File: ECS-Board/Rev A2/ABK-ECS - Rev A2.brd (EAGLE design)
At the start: 100 x 80 mm, 242 parts, among them J1 22-27-2061-06, J10 22-05-7068-06, J2 USB-B-S-RA, J3 1241050-5, J4 MSTBA2, J5 22-05-7068-06, J6 22-05-7028-02, J7 22-05-7058-05, J8 22-05-7068-06, J9 22-05-7028-02, K1 G6K-2G-Y, SW1 B3FS-1015, SW2 B3FS-1015, T1 EXMACHINA-LOGO-NAME, T10 MMBT2222AL, T11 MMBT2222AL, T12 IRLML5103TRPBF, T13 IRLML5103TRPBF, T14 IRLML5103TRPBF, T15 IRLML5103TRPBF, T16 MMBT2222AL, T17 MMBT2222AL, T18 MMBT2222AL, T19 MMBT2222AL, T2 IRLML5103TRPBF, T3 MMBT2222AL, T4 IRLML5103TRPBF, T5 IRLML5103TRPBF, T6 IRLML5103TRPBF, T7 IRLML5103TRPBF, T8 MMBT2222AL, T9 MMBT2222AL, U1 AT24C512C-SSHM-B, U2 LPC1768FBD100, U3 LT3686HDDPBF, U4 LT3686HDDPBF, U5 SN74LVC2G17DBVR, U6 SN74LVC2G17DBVR, U7 SN74LVC2G17DBVR, U8 SN74LVC2G17DBVR, U9 TC1264-3.3, X1 FC-135, X2 ASE-12, X3 3000

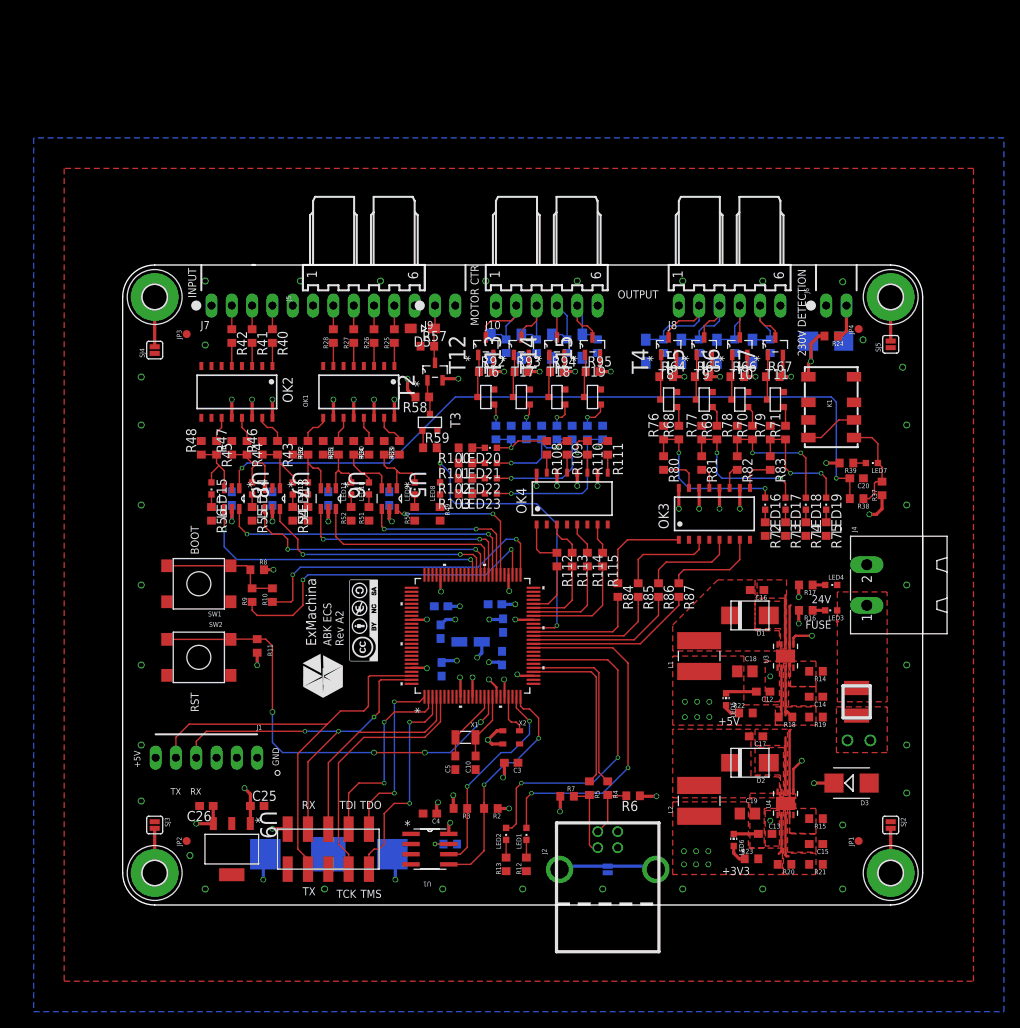
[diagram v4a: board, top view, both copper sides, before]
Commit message: Add pullup resistor on AT24C WP Separate +5V from ISP connector and the +5V general and add a diode Change +5V--->+3V3 conversion methode on input Wired OK2D
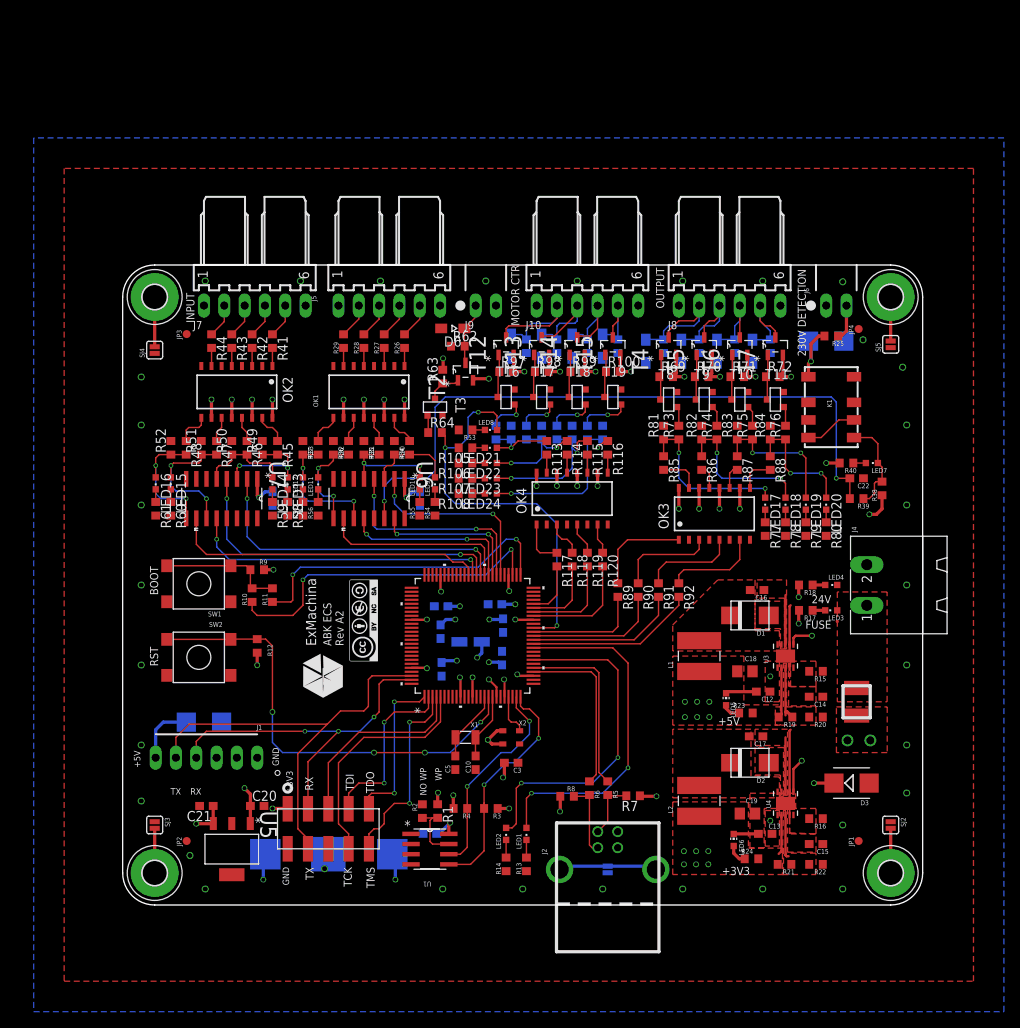
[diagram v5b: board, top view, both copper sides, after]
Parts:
- removed C25, C26: 1u, rcl:C0603
- removed U8: SN74LVC2G17DBVR, ti:SOT95P280X145-6N
- removed U9: TC1264-3.3, microchip-6:SOT230P700X180-4N
- added D14: 1N4148WS, diode:SOD323-W
- added LED24: Blue, led:CHIPLED_0603
- added R116: 1K, rcl:R0603
- added R117, R118, R119, R120: 330, rcl:R0603
- C20, C21: value 0.1uF -> 1u
- D5: value 1N4148WS -> STPS3L40UF; device diode:SOD323-W -> diode:SMB
- J7: value 22-05-7058-05 -> 22-05-7068-06; device con-molex:7395-05 -> con-molex:7395-06
- R100, R72: value 1K5 -> 330
- R101, R102, R103, R39, R73, R74, R75: value 1K5 -> 100
- R104, R76: value 4K7 -> 100
- R105, R106, R107, R77, R78, R79: value 4K7 -> 1K5
- R108, R40, R80: value 1K -> 1K5
- R109, R110, R111, R81, R82, R83: value 1K -> 4K7
- R11: value 10K -> 0R
- R112, R84: value 330 -> 4K7
- R113, R114, R115, R85, R86, R87: value 330 -> 1K
- R12, R22: value 1K5 -> 10K
- R14: value 31K6 -> 1K5
- R16: value 4K7 -> 31K6
- R18: value 52K3 -> 4K7
- R19: value 10K -> 52K3
- R20: value 31K6 -> 10K
- R21: value 10K -> 31K6
- R24, R59: value 100 -> 1K5
- R25: value 1K -> 100
- R33, R46, R47, R48: value 4K7 -> 1K
- R38: value 100 -> 4K7
- R4: value 33 -> 4K7
- R49, R50, R51, R52: value 1K5 -> 4K7
- R57, R60, R61, R8: value 10K -> 1K5
- R58: value 330 -> 1K5
- R6: value 1K5 -> 33
- R63, R89, R90, R91: value 10K -> 330
- R64: value 330 -> 100
- R65, R66, R67, R93, R94, R95: value 330 -> 10K
- R68, R96: value 100 -> 10K
- R69, R70, R71, R97, R98, R99: value 100 -> 330
- R88: value 10K -> 1K
- R9: value 0R -> 10K
- U5: value SN74LVC2G17DBVR -> TC1264-3.3; device ti:SOT95P280X145-6N -> microchip-6:SOT230P700X180-4N
- U6, U7: value SN74LVC2G17DBVR -> CD4050BD; device ti:SOT95P280X145-6N -> ti:SOIC127P600X175-16N
- moved D4 91.2 mm to (10.2, 22.9)
- moved C20 85.4 mm to (16.8, 12.4)
- moved C22 78.1 mm to (91.7, 53.3), flipped to the top, turned to 0 degrees
- moved LED16 76.2 mm to (4.13, 52.7)
- moved R40 73.5 mm to (90.5, 55.2), turned to 180 degrees
- moved R37 72.6 mm to (22.5, 57.1)
- moved R61 70.9 mm to (4.13, 49.5), flipped to the top, turned to 270 degrees
- moved R24 66.1 mm to (78.6, 5.78), turned to 0 degrees
- moved R60 64.9 mm to (6.02, 49.5), flipped to the top, turned to 270 degrees
- moved R25 54.6 mm to (88.6, 71.1), turned to 180 degrees
- moved D5 50.5 mm to (87.9, 70.5), flipped to the bottom
- moved U5 48.0 mm to (13.6, 6.99)
- moved R8 48.0 mm to (55.5, 13.6)
- moved R14 45.6 mm to (47.9, 5.08), turned to 270 degrees
- moved C21 44.7 mm to (10.5, 12.4), flipped to the top, turned to 180 degrees
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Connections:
- removed net INPUT: LED15.A, R45.2, R48.1, U8.3
- removed net INPUT_MCU: U2.63, U8.4
- new net +5V/1: C20.1, D4.C, J1.6, U5.1
- new net INPUT1: LED15.A, R47.2, R51.1, U7.11
- new net INPUT1_MCU: U2.63, U7.12
- new net INPUT2: LED16.A, R48.2, R52.1, U7.9
- new net INPUT2_MCU: U2.64, U7.10
- new net N$110: OK2.9, R48.1
- new net N$111: OK2.7, R44.2
- new net N$112: J7.2, R44.1
- new net N$90: LED16.C, R61.1
- net !RESET: now also R12.1; no longer R11.1
- net +24V: now also R100.2, R18.2, R63.2, R69.2, R70.2, R71.2, R72.2, R97.2, R98.2, R99.2; no longer R16.2, R58.2, R64.2, R65.2, R66.2, R67.2, R92.2, R93.2, R94.2, R95.2
- net +3V3: now also R1.1, R12.2, R21.2, R24.2, R4.2, R8.1, R9.2, U5.3, U6.1, U7.1; no longer C22.1, C26.1, R11.2, R2.2, R20.2, R23.2, R6.1, R8.2, U5.5, U6.5, U7.5, U8.5, U9.3
- net +5V: now also OK2.10, R19.2, R23.2, R38.1, R40.2; no longer C25.1, J1.6, R18.2, R22.2, R37.1, R39.2, U9.1
- net 230V_DETECTION: now also C22.1, R39.2, U6.14; no longer C20.1, R38.2, U8.1
- net 230V_DETECTION_MCU: now also U6.15; no longer U8.6
- net BOOT_SELECT_P2_10: now also R10.1; no longer R9.1
- net BOOT_SELECT_P2_12: now also R11.1; no longer R10.1
- net BRAKE_CONTROL: now also D10.C, R68.2; no longer D9.C, R63.2
- net BRAKE_CONTROL_MCU: now also R92.2; no longer R87.2
- net CLUTCH_CONTROL: now also D9.C, R67.2; no longer D8.C, R62.2
- net CLUTCH_CONTROL_MCU: now also R91.2; no longer R86.2
- net DRIVE_STATUS_1: now also R32.2, R36.1, U6.9; no longer R31.2, R35.1, U6.1
- net DRIVE_STATUS_1_MCU: now also U6.10; no longer U6.6
- net DRIVE_STATUS_2: now also R33.2, R37.1, U6.11; no longer R32.2, R36.1, U6.3
- net DRIVE_STATUS_2_MCU: now also U6.12; no longer U6.4
- net EEPROM_SCL: now also R4.1; no longer R3.1
- net EEPROM_SDA: now also R3.1; no longer R2.1
- net EMERGENCY_STOP: now also R30.2, R34.1, U6.3; no longer R29.2, R33.1, U5.1
- net EMERGENCY_STOP_MCU: now also U6.2; no longer U5.6
- net GND: now also D14.A, J7.6, OK2.8, R108.2, R109.2, R110.2, R111.2, R112.2, R14.2, R16.1, R2.2, R20.1, R22.1, R37.2, R57.2, R58.2, R59.2, R60.2, R61.2, R65.1, R66.1, R67.1, R68.1, R80.2, R81.2, R82.2, R83.2, R84.2, R93.1, R94.1, R95.1, R96.1, U5.4, U6.8, U7.8; no longer C25.2, C26.2, J7.5, R1.2, R100.2, R101.2, R102.2, R103.2, R104.2, R12.2, R14.1, R19.1, R21.1, R33.2, R46.2, R47.2, R48.2, R57.1, R60.1, R61.1, R63.1, R72.2, R73.2, R74.2, R75.2, R76.2, R88.1, R89.1, R90.1, R91.1, U6.2, U7.2, U8.2, U9.2, U9.4
- net LED1: now also D11.C, R93.2; no longer D10.C, R88.2
- net LED1_MCU: now also R117.2; no longer R112.2
- net LED2: now also D12.C, R94.2; no longer D11.C, R89.2
- net LED2_MCU: now also R118.2; no longer R113.2
- net LED3: now also D13.C, R95.2; no longer D12.C, R90.2
- net LED3_MCU: now also R119.2; no longer R114.2
- net LED4: now also D14.C, R96.2; no longer D13.C, R91.2
- net LED4_MCU: now also R120.2; no longer R115.2
- net LIMIT_SWITCH: now also R31.2, R35.1, U6.5; no longer R30.2, R34.1, U5.3
- net LIMIT_SWITCH_MCU: now also U6.4; no longer U5.4
- net L_VALIDATION: now also D8.C, R66.2; no longer D7.C, R61.2
- net L_VALIDATION_MCU: now also R90.2; no longer R85.2
- net MOTOR_CONTROL_MCU: now also R64.2; no longer R59.2
- net N$1: now also R6.1, R8.2; no longer R5.1, R7.2
- net N$100: now also R45.1; no longer R43.1
- net N$101: now also R42.2; no longer R41.2
- net N$102: now also J7.4, R42.1; no longer J7.3, R41.1
- net N$103: now also R46.1; no longer R44.1
- net N$104: now also R43.2; no longer R42.2
- net N$105: now also J7.3, R43.1; no longer J7.2, R42.1
- net N$106: now also R47.1; no longer R45.1
- net N$107: now also R58.1; no longer R54.1
- net N$108: now also R59.1; no longer R55.1
- net N$109: now also R60.1; no longer R56.1
- net N$13: now also R21.1, R22.2; no longer R20.1, R21.2
- net N$17: now also R73.2; no longer R68.2
- net N$18: now also R69.1; no longer R64.1
- net N$19: now also R74.2; no longer R69.2
- net N$2: now also R5.1, R7.2; no longer R4.1, R6.2
- net N$20: now also R70.1; no longer R65.1
- net N$21: now also R75.2; no longer R70.2
- net N$22: now also R71.1; no longer R66.1
- net N$23: now also R76.2; no longer R71.2
- net N$24: now also R72.1; no longer R67.1
- net N$25: now also R64.1; no longer R59.1
- net N$26: now also R63.1; no longer R58.1
- net N$27: now also R1.2, R2.1; no longer R1.1
- net N$28: now also D5.C, R25.2; no longer D4.C, R24.2
- net N$29: now also R13.1; no longer R12.1
- net N$3: now also R14.1; no longer R13.1
- net N$30: now also D6.C, R62.2; no longer D5.C, R57.2
- net N$31: now also LED21.A, R101.1, R109.1, R113.1; no longer LED20.A, R104.1, R108.1, R96.1
- net N$32: now also R25.1; no longer R24.1
- net N$33: now also R113.2; no longer R108.2
- net N$34: now also LED22.A, R102.1, R110.1, R114.1; no longer LED21.A, R105.1, R109.1, R97.1
- net N$35: now also R114.2; no longer R109.2
- net N$36: now also LED23.A, R103.1, R111.1, R115.1; no longer LED22.A, R106.1, R110.1, R98.1
- net N$37: now also LED24.A, R104.1, R112.1, R116.1; no longer LED23.A, R107.1, R111.1, R99.1
- net N$38: now also R115.2; no longer R110.2
- net N$39: now also R116.2; no longer R111.2
- net N$4: now also R15.2; no longer R14.2
- net N$40: now also R117.1; no longer R112.1
- net N$41: now also R26.2; no longer R25.2
- net N$42: now also R118.1; no longer R113.1
- net N$43: now also R120.1; no longer R115.1
- net N$44: now also R18.1; no longer R17.1
- net N$45: now also R17.1; no longer R16.1
- net N$46: now also R119.1; no longer R114.1
- net N$47: now also R27.2; no longer R26.2
- net N$48: now also R28.2; no longer R27.2
- net N$49: now also R29.2; no longer R28.2
- net N$5: now also R11.2, R9.1; no longer R8.1, R9.2
- net N$50: now also R24.1; no longer R23.1
- net N$51: now also R23.1; no longer R22.1
- net N$52: now also R29.1; no longer R28.1
- net N$53: now also R28.1; no longer R27.1
- net N$54: now also R27.1; no longer R26.1
- net N$55: now also R26.1; no longer R25.1
- net N$56: now also R53.1; no longer R49.1
- net N$57: now also R54.1; no longer R50.1
- net N$58: now also R55.1; no longer R51.1
- net N$59: now also R56.1; no longer R52.1
- net N$61: now also R33.1; no longer R32.1
- net N$62: now also R32.1; no longer R31.1
- net N$63: now also R31.1; no longer R30.1
- net N$64: now also R30.1; no longer R29.1
- net N$65: now also R57.1; no longer R53.1
- net N$66: now also LED21.C, R105.1; no longer LED20.C, R100.1
- net N$67: now also LED22.C, R106.1; no longer LED21.C, R101.1
- net N$68: now also LED23.C, R107.1; no longer LED22.C, R102.1
- net N$69: now also LED24.C, R108.1; no longer LED23.C, R103.1
- net N$7: now also R16.2; no longer R15.2
- net N$71: now also R97.1; no longer R92.1
- net N$72: now also R98.1; no longer R93.1
- net N$73: now also R38.2, R39.1; no longer R37.2, R38.1
- net N$74: now also R40.1; no longer R39.1
- net N$75: now also LED17.A, R73.1, R81.1, R85.1; no longer LED16.A, R68.1, R76.1, R80.1
- net N$76: now also R85.2; no longer R80.2
- net N$77: now also R99.1; no longer R94.1
- net N$78: now also R100.1; no longer R95.1
- net N$79: now also LED18.A, R74.1, R82.1, R86.1; no longer LED17.A, R69.1, R77.1, R81.1
- net N$80: now also R86.2; no longer R81.2
- net N$81: now also R41.2; no longer R40.2
- net N$82: now also J7.5, R41.1; no longer J7.4, R40.1
- net N$83: now also LED19.A, R75.1, R83.1, R87.1; no longer LED18.A, R70.1, R78.1, R82.1
- net N$84: now also R101.2; no longer R96.2
- net N$85: now also R102.2; no longer R97.2
- net N$86: now also LED20.A, R76.1, R84.1, R88.1; no longer LED19.A, R71.1, R79.1, R83.1
- net N$87: now also R87.2; no longer R82.2
- net N$88: now also R88.2; no longer R83.2
- net N$89: now also R89.1; no longer R84.1
- net N$9: now also R19.1, R20.2; no longer R18.1, R19.2
- net N$91: now also R90.1; no longer R85.1
- net N$92: now also R92.1; no longer R87.1
- net N$93: now also R91.1; no longer R86.1
- net N$94: now also LED17.C, R77.1; no longer LED16.C, R72.1
- net N$95: now also LED18.C, R78.1; no longer LED17.C, R73.1
- net N$96: now also LED19.C, R79.1; no longer LED18.C, R74.1
- net N$97: now also LED20.C, R80.1; no longer LED19.C, R75.1
- net N$98: now also R103.2; no longer R98.2
- net N$99: now also R104.2; no longer R99.2
- net R_VALIDATION: now also D7.C, R65.2; no longer D6.C, R60.2
- net R_VALIDATION_MCU: now also R89.2; no longer R84.2
- net SLOWFEED_1: now also R45.2, R49.1, U7.3; no longer R43.2, R46.1, U7.1
- net SLOWFEED_1_MCU: now also U2.61, U7.2; no longer U2.62, U7.6
- net SLOWFEED_2: now also R46.2, R50.1, U7.5; no longer R44.2, R47.1, U7.3
- net SLOWFEED_2_MCU: now also U2.62; no longer U2.61
- net USB_D_N: now also R5.2; no longer R4.2
- net USB_D_P: now also R6.2; no longer R5.2
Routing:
- net +5V: track 110.8 -> 46.9 mm
- net INPUT2_MCU: track 0.00 -> 39.4 mm
- net INPUT_MCU: track 38.2 -> 0.00 mm, vias 2 -> 0
- net INPUT1_MCU: track 0.00 -> 38.0 mm, vias 0 -> 2
- net +5V/1: track 0.00 -> 27.0 mm, vias 0 -> 1
- net 230V_DETECTION_MCU: track 39.0 -> 18.8 mm
- net INPUT1: track 0.00 -> 18.3 mm, vias 0 -> 2
- net INPUT2: track 0.00 -> 16.4 mm, vias 0 -> 2
- net MOTOR_CONTROL_MCU: track 39.9 -> 50.8 mm, vias 2 -> 3
- net 230V_DETECTION: track 94.6 -> 83.8 mm
- net SLOWFEED_1_MCU: track 30.9 -> 39.9 mm
- net INPUT: track 9.01 -> 0.00 mm
- net SLOWFEED_2_MCU: track 33.9 -> 41.8 mm
- net DRIVE_STATUS_2: track 9.57 -> 17.0 mm, vias 0 -> 2
- net DRIVE_STATUS_2_MCU: track 28.8 -> 21.9 mm
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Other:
- board text added: "NO WP"
- board text added: "WP"

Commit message: Resize and place all name and value of the component of the board
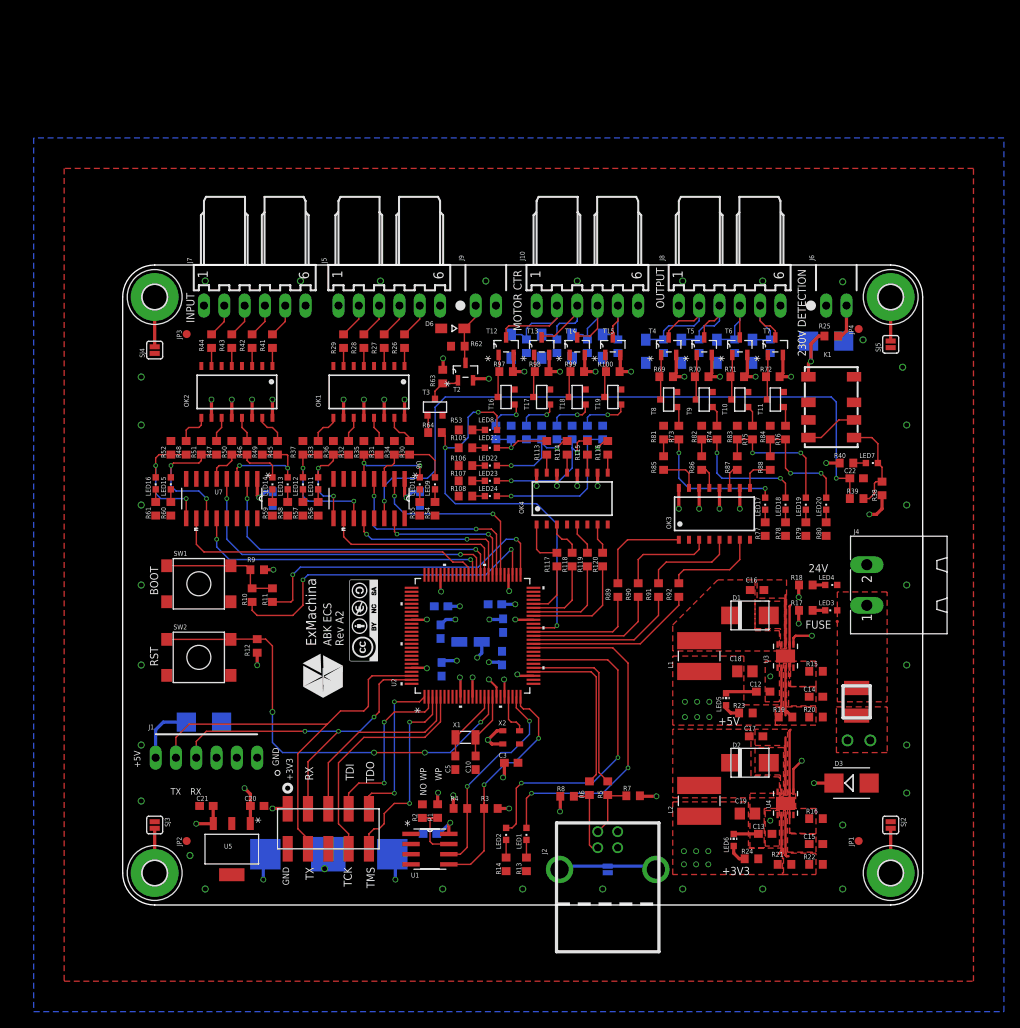
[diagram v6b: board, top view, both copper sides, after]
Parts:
- moved LED23 0.32 mm to (46.0, 53.0)
- moved LED24 0.32 mm to (46.0, 51.1)
- moved R107 0.32 mm to (42.9, 53.0)
- moved R108 0.32 mm to (42.9, 51.1)
- moved LED22 0.32 mm to (46.0, 54.9)
- moved R106 0.32 mm to (42.9, 54.9)

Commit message: Final modifications before production version:
* Rename inputs and outputs to generic names
* Add silkscreen labels
* Move components for better layout in output block
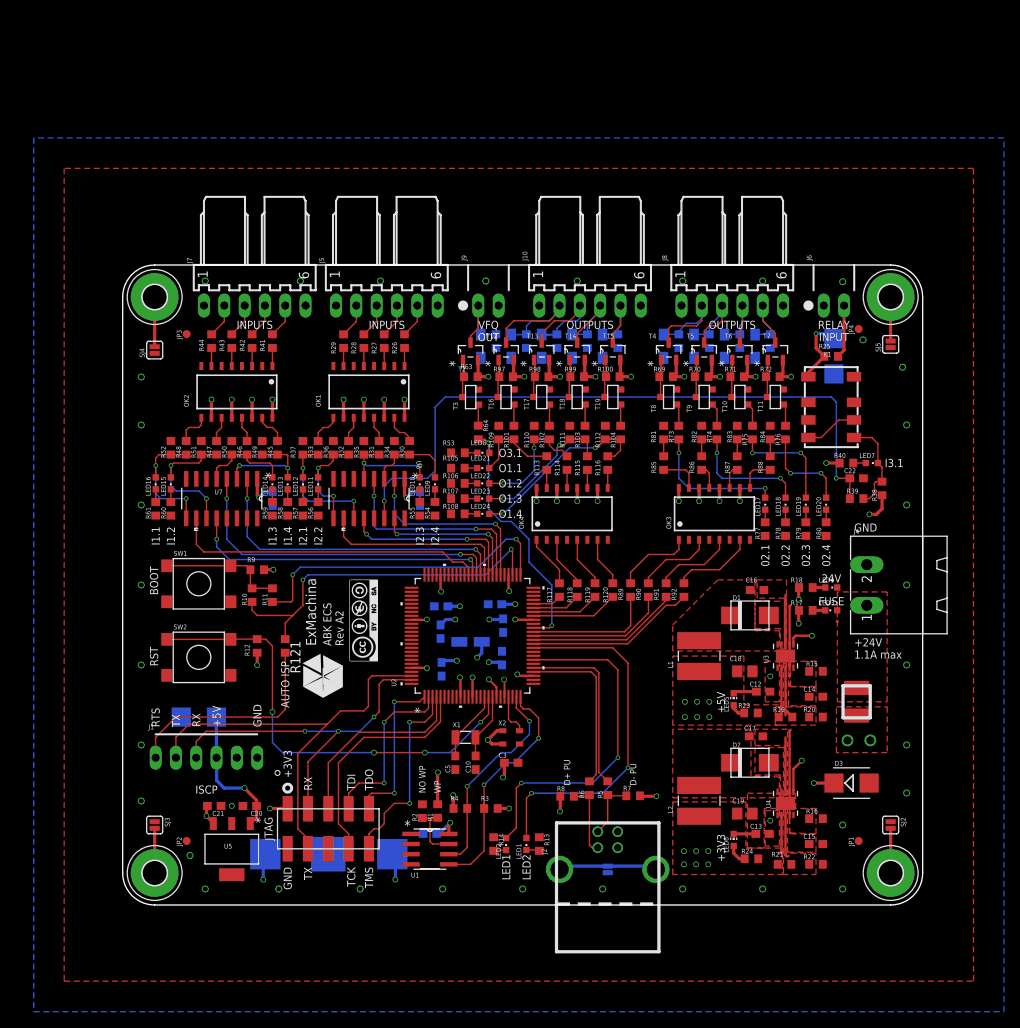
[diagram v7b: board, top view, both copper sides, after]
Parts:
- added R121: 0R, rcl:R0603
- LED21: value Blue -> 01.1
- moved R64 5.41 mm to (44.5, 59.1), turned to 270 degrees
- moved R62 4.80 mm to (46.7, 70.5), flipped to the bottom, turned to 90 degrees
- moved T3 4.63 mm to (43.5, 63.5), turned to 270 degrees
- moved R104 4.15 mm to (62.2, 59.1), flipped to the top
- moved D6 4.14 mm to (44.8, 69.8), flipped to the bottom, turned to 270 degrees
- moved R120 4.02 mm to (61.3, 39.4)
- moved R119 3.93 mm to (59.0, 39.4)
- moved R118 3.86 mm to (56.8, 39.4)
- moved R117 3.82 mm to (54.6, 39.4)
- moved R103 3.52 mm to (57.8, 59.1), flipped to the top
- moved R63 3.51 mm to (43.5, 66.0), turned to 0 degrees
- moved LED8 3.01 mm to (45.1, 56.5)
- moved R53 3.01 mm to (41.9, 56.5)
- moved R13 3.01 mm to (52.1, 7.62), turned to 90 degrees
- moved R14 2.98 mm to (46.4, 7.62), turned to 90 degrees
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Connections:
- net 230V_DETECTION renamed INPUT3.1
- net 230V_DETECTION_MCU renamed INPUT3.1_MCU
- net BRAKE_CONTROL renamed OUTPUT2.4
- net BRAKE_CONTROL_MCU renamed OUTPUT2.4_MCU
- net CLUTCH_CONTROL renamed OUTPUT2.3
- net CLUTCH_CONTROL_MCU renamed OUTPUT2.3_MCU
- net DRIVE_STATUS_1 renamed INPUT2.2
- net DRIVE_STATUS_1_MCU renamed INPUT2.2_MCU
- net DRIVE_STATUS_2 renamed INPUT2.1
- net DRIVE_STATUS_2_MCU renamed INPUT2.1_MCU
- net EMERGENCY_STOP renamed INPUT2.4
- net EMERGENCY_STOP_MCU renamed INPUT2.4_MCU
- net INPUT1 renamed INPUT1.2
- net INPUT1_MCU renamed INPUT1.2_MCU
- net INPUT2 renamed INPUT1.1
- net INPUT2_MCU renamed INPUT1.1_MCU
- net LED1 renamed OUTPUT1.1
- net LED1_MCU renamed OUTPUT1.1_MCU
- net LED2 renamed OUTPUT1.2
- net LED2_MCU renamed OUTPUT1.2_MCU
- net LED3 renamed OUTPUT1.3
- net LED3_MCU renamed OUTPUT1.3_MCU
- net LED4 renamed OUTPUT1.4
- net LED4_MCU renamed OUTPUT1.4_MCU
- net LED_DEBUG renamed ONBOARD_LED2
- net LIMIT_SWITCH renamed INPUT2.3
- net LIMIT_SWITCH_MCU renamed INPUT2.3_MCU
- net L_VALIDATION renamed OUTPUT2.2
- net L_VALIDATION_MCU renamed OUTPUT2.2_MCU
- net MOTOR_CONTROL_MCU renamed OUTPUT3.2_MCU
- net N$30 renamed MOTOR_VFQ
- net R_VALIDATION renamed OUTPUT2.1
- net R_VALIDATION_MCU renamed OUTPUT2.1_MCU
- net SLOWFEED_1 renamed INPUT1.4
- net SLOWFEED_1_MCU renamed INPUT1.4_MCU
- net SLOWFEED_2 renamed INPUT1.3
- net SLOWFEED_2_MCU renamed INPUT1.3_MCU
- net USB_UP_LED renamed ONBOARD_LED1
- new net ISP_RTS: J1.6, R121.2
- net +5V/1: now also J1.3; no longer J1.6
- net BOOT_SELECT_P2_10: now also R121.1
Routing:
- net ISP_RTS: track 0.00 -> 27.3 mm
- net OUTPUT3.2_MCU: track 50.8 -> 32.0 mm, vias 3 -> 2
- net N$99: track 6.80 -> 2.67 mm, vias 1 -> 0
- net +5V: track 46.9 -> 43.1 mm
- net OUTPUT1.3_MCU: track 11.9 -> 8.47 mm
- net OUTPUT1.2_MCU: track 9.46 -> 6.04 mm
- net +24V: track 50.1 -> 46.8 mm, vias 19 -> 18
- net OUTPUT1.1_MCU: track 6.97 -> 3.61 mm
- net BOOT_SELECT_P2_10: track 42.2 -> 45.6 mm
- net OUTPUT1.4_MCU: track 14.1 -> 10.9 mm
- net N$98: track 5.79 -> 2.67 mm, vias 1 -> 0
- net OUTPUT1.2: track 15.2 -> 18.3 mm
- net MOTOR_VFQ: track 7.80 -> 10.7 mm
- net N$85: track 5.53 -> 2.67 mm, vias 1 -> 0
- net N$91: track 12.3 -> 9.75 mm
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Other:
- board text added: "+24V 1.1A max"
- board text added: "02.1"
- board text added: "02.2"
- board text added: "02.3"
- board text added: "02.4"
- board text added: "AUTO ISP"
- board text added: "CR1220 3V"
- board text added: "D+ PU"
- board text added: "D- PU"
- board text added: "I1.1"
- board text added: "I1.2"
- board text added: "I1.3"
- board text added: "I1.4"
- board text added: "I2.1"
- board text added: "I2.2"
- board text added: "I2.3"
- board text added: "I2.4"
- board text added: "I3.1"
- board text added: "INPUTS"
- board text added: "ISCP"
- board text added: "JTAG"
- board text added: "LED1"
- board text added: "LED2"
- board text added: "O1.1"
- board text added: "O1.2"
- board text added: "O1.3"
- board text added: "O1.4"
- board text added: "O3.1"
- board text added: "OUTPUTS"
- board text added: "RELAY INPUT"
- board text added: "RTS"
- board text added: "VFQ OUT"
- board text removed: "230V DETECTION"
- board text removed: "INPUT"
- board text removed: "MOTOR CTR"
- board text removed: "OUTPUT"
